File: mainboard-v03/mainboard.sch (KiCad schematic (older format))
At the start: 0 parts

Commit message: schematic organizing
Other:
- note removed: "DRDY pins on XTB\nADD BREAKOUT AREA\nCONFIRM GPS SCHEME\n\n"
- note removed: "TO DO"
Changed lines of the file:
@@
 F1 "Burn_Wires.sch" 50
 $EndSheet
-Text Notes 1850 1850 0    100  ~ 0
-TO DO
-Text Notes 1850 2550 0    100  ~ 0
-DRDY pins on XTB\nADD BREAKOUT AREA\nCONFIRM GPS SCHEME\n\n
 $EndSCHEMATC

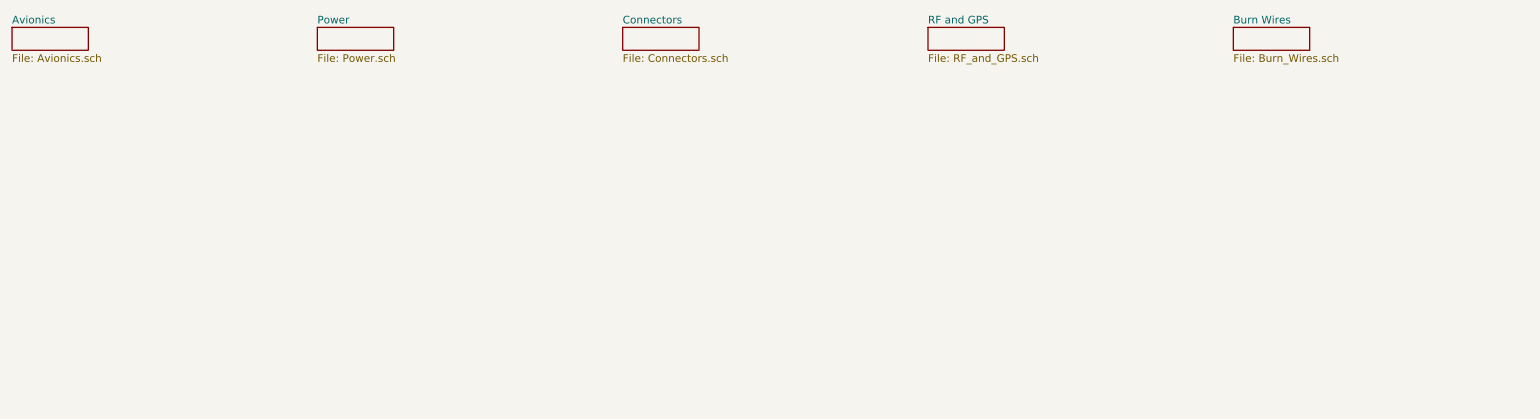
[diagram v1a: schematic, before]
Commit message: cleaning up schematic scheets
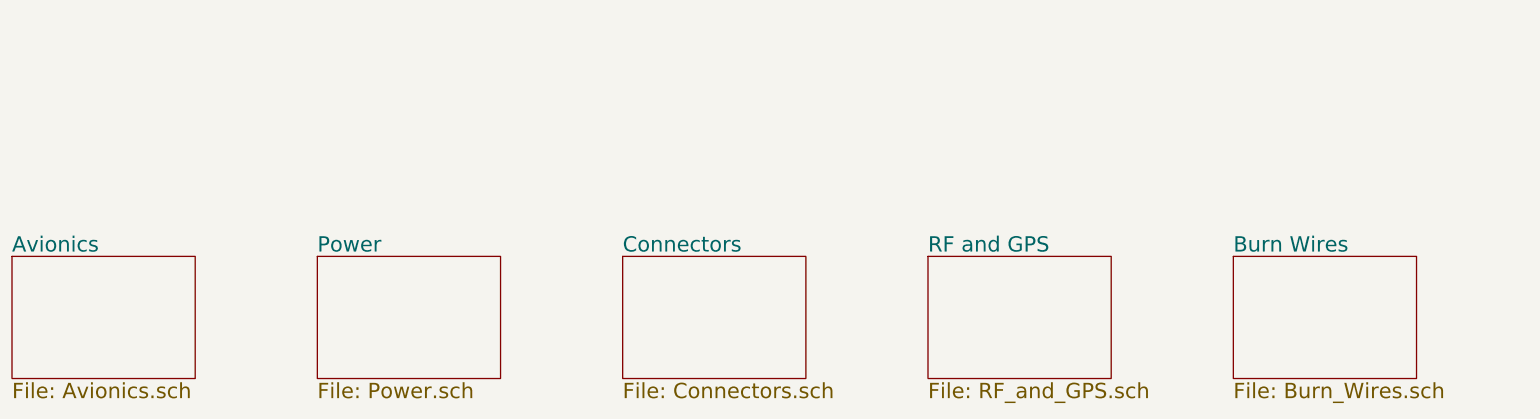
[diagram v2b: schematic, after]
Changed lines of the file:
@@
 Title "PyCubed Mainboard"
 Date ""
-Rev "v02"
+Rev "v03"
 Comp "Stanford University"
 Comment1 "rexlab.stanford.edu"
@@
 $EndDescr
 $Sheet
-S 1000 1000 500  150
-U 5CEC5A72
-F0 "Avionics" 50
-F1 "Avionics.sch" 50
+S 9000 2500 1200 800
+U 5CEC6476
+F0 "Burn Wires" 100
+F1 "Burn_Wires.sch" 100
 $EndSheet
 $Sheet
-S 3000 1000 500  150
-U 5CEC5DDE
-F0 "Power" 50
-F1 "Power.sch" 50
+S 7000 2500 1200 800
+U 5CEC6281
+F0 "RF and GPS" 100
+F1 "RF_and_GPS.sch" 100
 $EndSheet
 $Sheet
-S 5000 1000 500  150
+S 5000 2500 1200 800
 U 5CEC60EB
-F0 "Connectors" 50
-F1 "Connectors.sch" 50
+F0 "Connectors" 100
+F1 "Connectors.sch" 100
 $EndSheet
 $Sheet
-S 7000 1000 500  150
-U 5CEC6281
-F0 "RF and GPS" 50
-F1 "RF_and_GPS.sch" 50
+S 3000 2500 1200 800
+U 5CEC5DDE
+F0 "Power" 100
+F1 "Power.sch" 100
 $EndSheet
 $Sheet
-S 9000 1000 500  150
-U 5CEC6476
-F0 "Burn Wires" 50
-F1 "Burn_Wires.sch" 50
+S 1000 2500 1200 800
+U 5CEC5A72
+F0 "Avionics" 100
+F1 "Avionics.sch" 100
 $EndSheet
 $EndSCHEMATC
